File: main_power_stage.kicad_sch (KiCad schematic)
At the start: 69 parts, among them SW1 CAS-120TA, U2 LV14540DDAR, U6 TPS65987DDHRSHR, U7 LV14540DDAR, U8 74CBTLV3257_VQFN, U9 W25Q80DV_SOIC-8

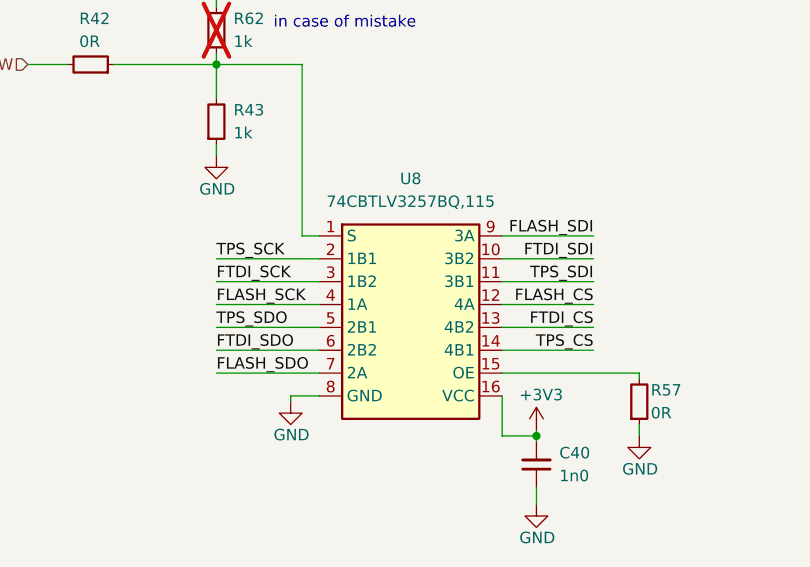
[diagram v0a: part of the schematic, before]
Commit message: [#62835] Start PWR plane placement
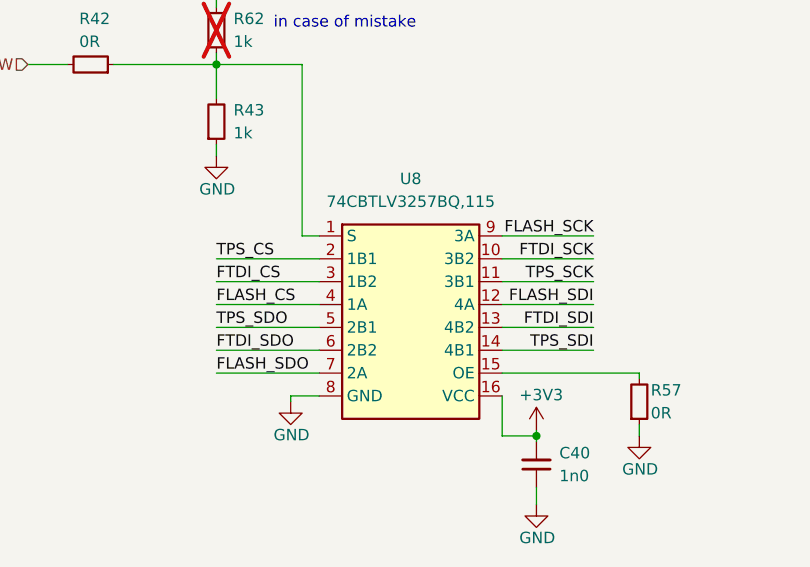
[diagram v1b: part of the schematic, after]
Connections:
- net FLASH_CS: now also U8.4 (1A); no longer U8.12 (4A)
- net FLASH_SCK: now also U8.9 (3A); no longer U8.4 (1A)
- net FLASH_SDI: now also U8.12 (4A); no longer U8.9 (3A)
- net FTDI_CS: now also U8.3 (1B2); no longer U8.13 (4B2)
- net FTDI_SCK: now also U8.10 (3B2); no longer U8.3 (1B2)
- net FTDI_SDI: now also U8.13 (4B2); no longer U8.10 (3B2)
- net TPS_CS: now also U8.2 (1B1); no longer U8.14 (4B1)
- net TPS_SCK: now also U8.11 (3B1); no longer U8.2 (1B1)
- net TPS_SDI: now also U8.14 (4B1); no longer U8.11 (3B1)
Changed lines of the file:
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@@
     (effects (font (size 1.27 1.27)) (justify right bottom))
   )
-  (label "FTDI_SCK" (at 111.76 246.38 0) (fields_autoplaced)
-    (effects (font (size 1.27 1.27)) (justify left bottom))
+  (label "FTDI_SCK" (at 153.67 243.84 180) (fields_autoplaced)
+    (effects (font (size 1.27 1.27)) (justify right bottom))
   )
   (label "TPS_SDI" (at 333.375 96.52 180) (fields_autoplaced)
@@
     (effects (font (size 1.27 1.27)) (justify right bottom))
   )
-  (label "FTDI_CS" (at 153.67 251.46 180) (fields_autoplaced)
-    (effects (font (size 1.27 1.27)) (justify right bottom))
+  (label "FTDI_CS" (at 111.76 246.38 0) (fields_autoplaced)
+    (effects (font (size 1.27 1.27)) (justify left bottom))
   )
   (label "FLASH_SDO" (at 180.975 243.84 0) (fields_autoplaced)
@@
     (effects (font (size 1.27 1.27)) (justify right bottom))
   )
-  (label "TPS_SDI" (at 153.67 246.38 180) (fields_autoplaced)
+  (label "TPS_SDI" (at 153.67 254 180) (fields_autoplaced)
     (effects (font (size 1.27 1.27)) (justify right bottom))
   )
-  (label "FLASH_SDI" (at 153.67 241.3 180) (fields_autoplaced)
+  (label "FLASH_SDI" (at 153.67 248.92 180) (fields_autoplaced)
     (effects (font (size 1.27 1.27)) (justify right bottom))
   )
@@
     (effects (font (size 1.27 1.27)) (justify right bottom))
   )
-  (label "TPS_CS" (at 153.67 254 180) (fields_autoplaced)
-    (effects (font (size 1.27 1.27)) (justify right bottom))
+  (label "TPS_CS" (at 111.76 243.84 0) (fields_autoplaced)
+    (effects (font (size 1.27 1.27)) (justify left bottom))
   )
-  (label "FLASH_CS" (at 153.67 248.92 180) (fields_autoplaced)
-    (effects (font (size 1.27 1.27)) (justify right bottom))
+  (label "FLASH_CS" (at 111.76 248.92 0) (fields_autoplaced)
+    (effects (font (size 1.27 1.27)) (justify left bottom))
   )
   (label "FTDI_TPS_rst" (at 394.97 27.94 180) (fields_autoplaced)
@@
     (effects (font (size 1.27 1.27)) (justify right bottom))
   )
-  (label "FLASH_SCK" (at 111.76 248.92 0) (fields_autoplaced)
-    (effects (font (size 1.27 1.27)) (justify left bottom))
+  (label "FLASH_SCK" (at 153.67 241.3 180) (fields_autoplaced)
+    (effects (font (size 1.27 1.27)) (justify right bottom))
   )
   (label "FTDI_TPS_rst" (at 226.06 80.01 0) (fields_autoplaced)
@@
     (effects (font (size 1.27 1.27)) (justify left bottom))
   )
-  (label "TPS_SCK" (at 111.76 243.84 0) (fields_autoplaced)
-    (effects (font (size 1.27 1.27)) (justify left bottom))
-  )
-  (label "FTDI_SDI" (at 153.67 243.84 180) (fields_autoplaced)
+  (label "TPS_SCK" (at 153.67 246.38 180) (fields_autoplaced)
     (effects (font (size 1.27 1.27)) (justify right bottom))
   )
+  (label "FTDI_SDI" (at 153.67 251.46 180) (fields_autoplaced)
+    (effects (font (size 1.27 1.27)) (justify right bottom))
+  )

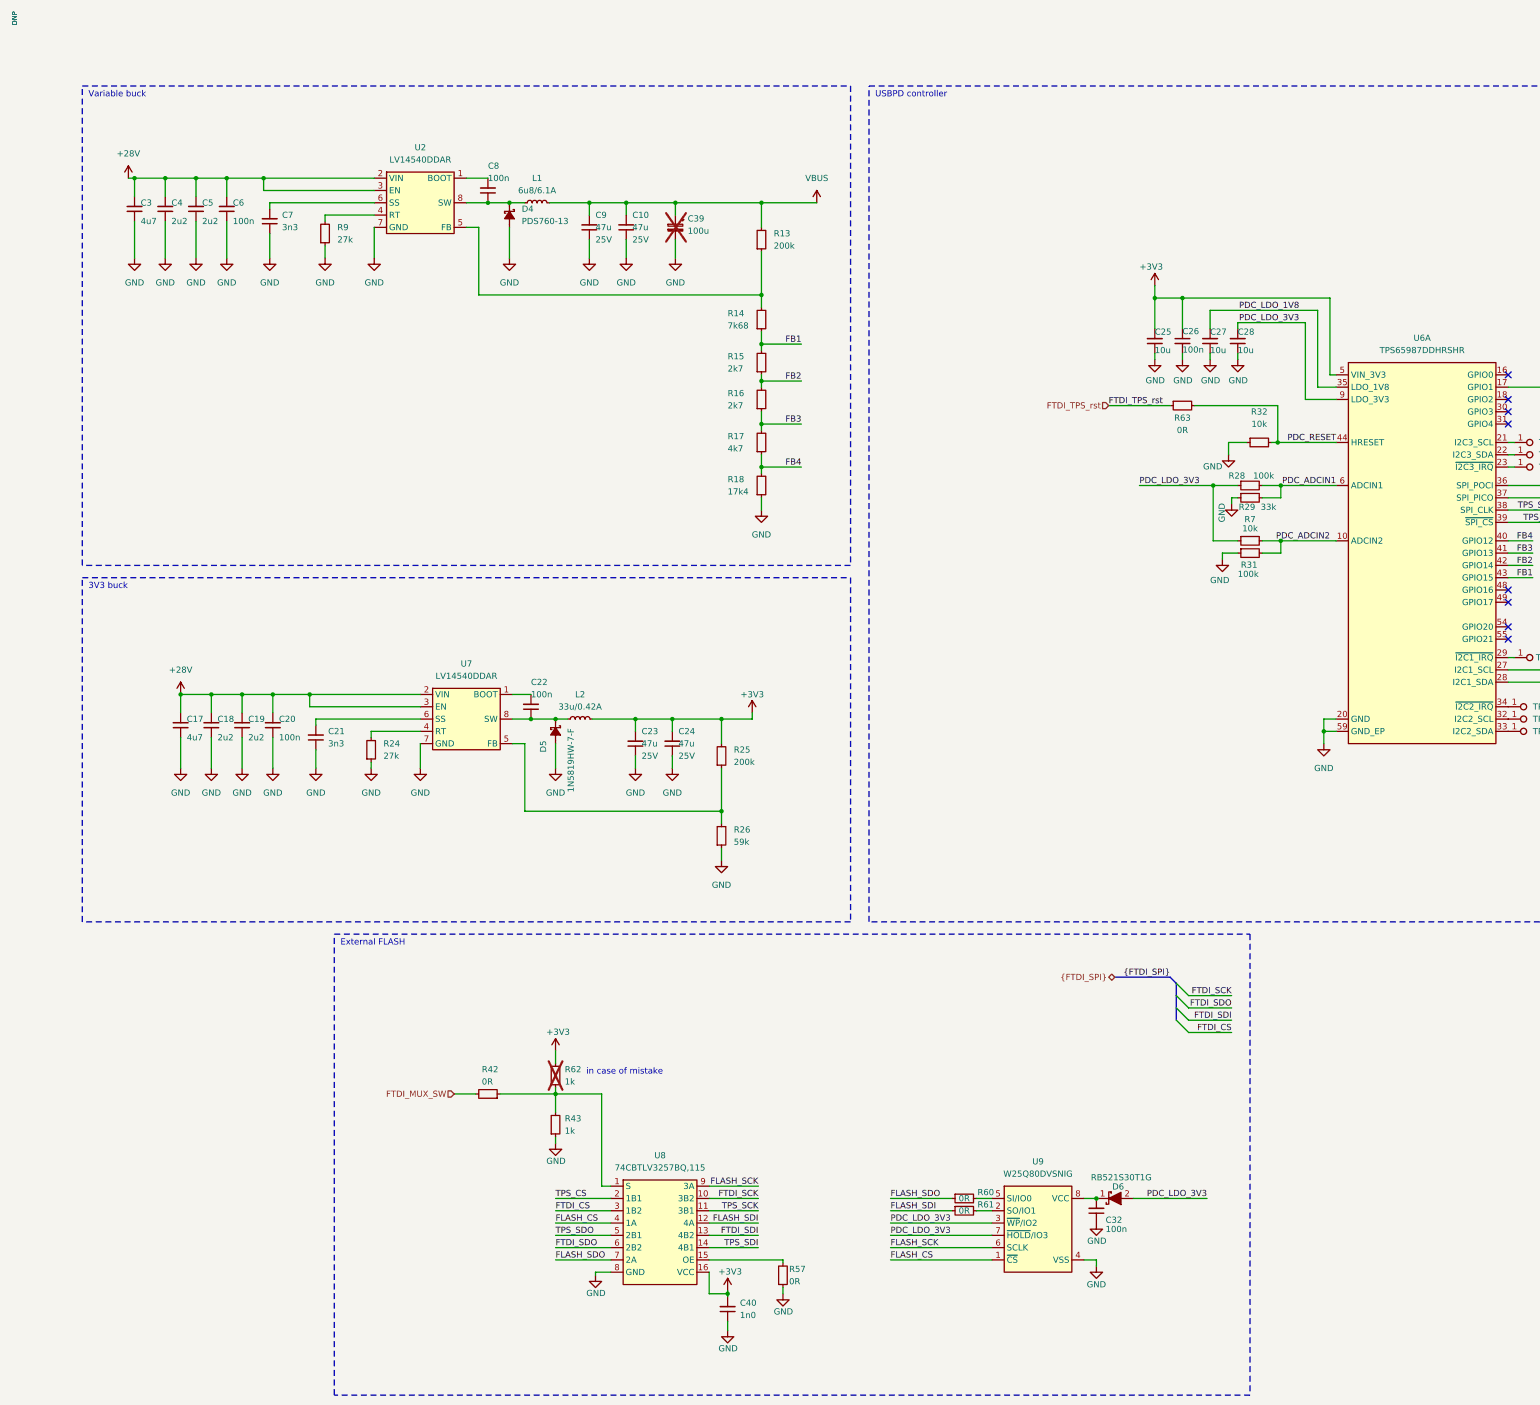
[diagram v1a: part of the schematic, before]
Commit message: [#62835] Tacle ERC problems, add PWR flags
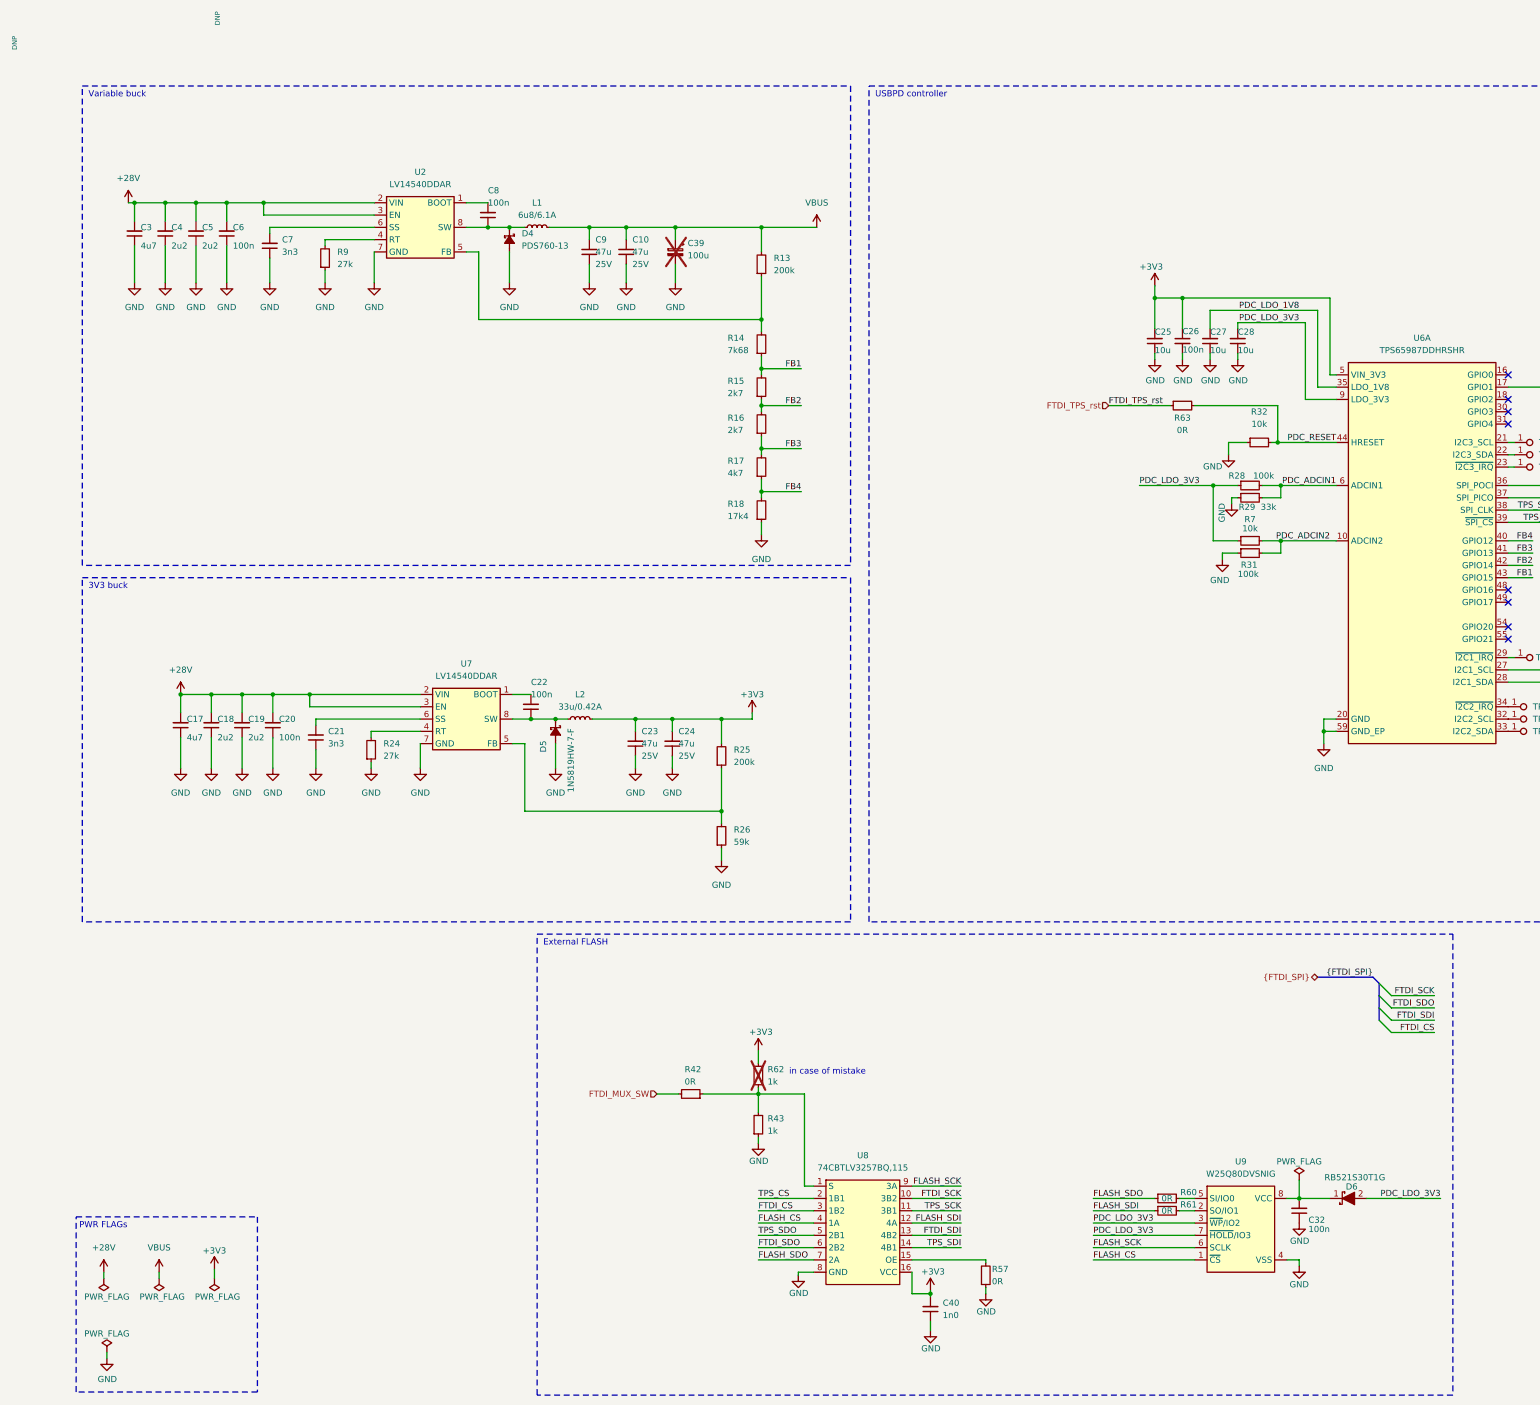
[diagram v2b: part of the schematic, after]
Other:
- note added: "PWR FLAGs"
- moved on the sheet: C10, C3, C32, C39, C4, C40, C5, C6, C7, C8, C9, D4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
